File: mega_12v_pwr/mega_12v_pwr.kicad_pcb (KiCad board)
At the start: 2 copper layers, 170 x 144 mm, 48 parts, among them J1 Conn_01x01, J10 Conn_01x01, J11 Conn_01x01, J12 Conn_01x01, J13 Conn_01x01, J14 Conn_01x01, J15 Conn_01x01, J16 Conn_01x01, J17 Conn_01x01, J18 Conn_01x01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

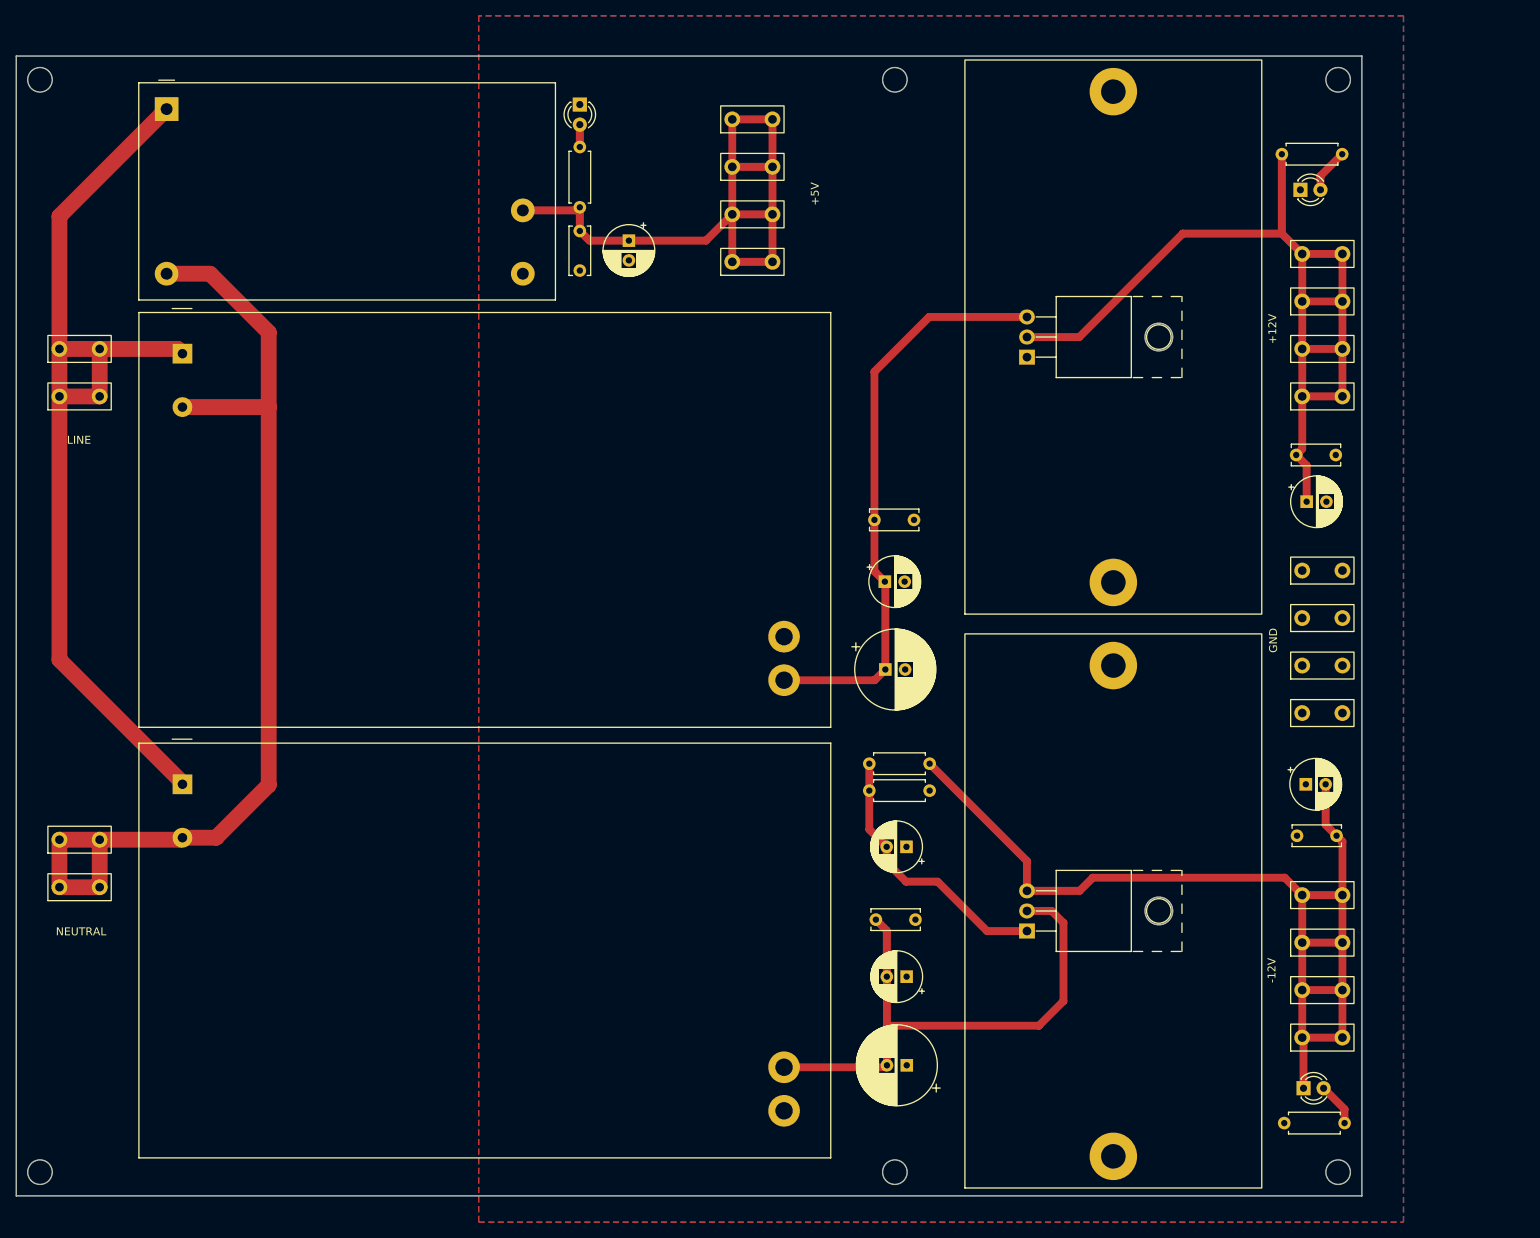
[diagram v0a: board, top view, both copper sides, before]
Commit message: Added fan connector
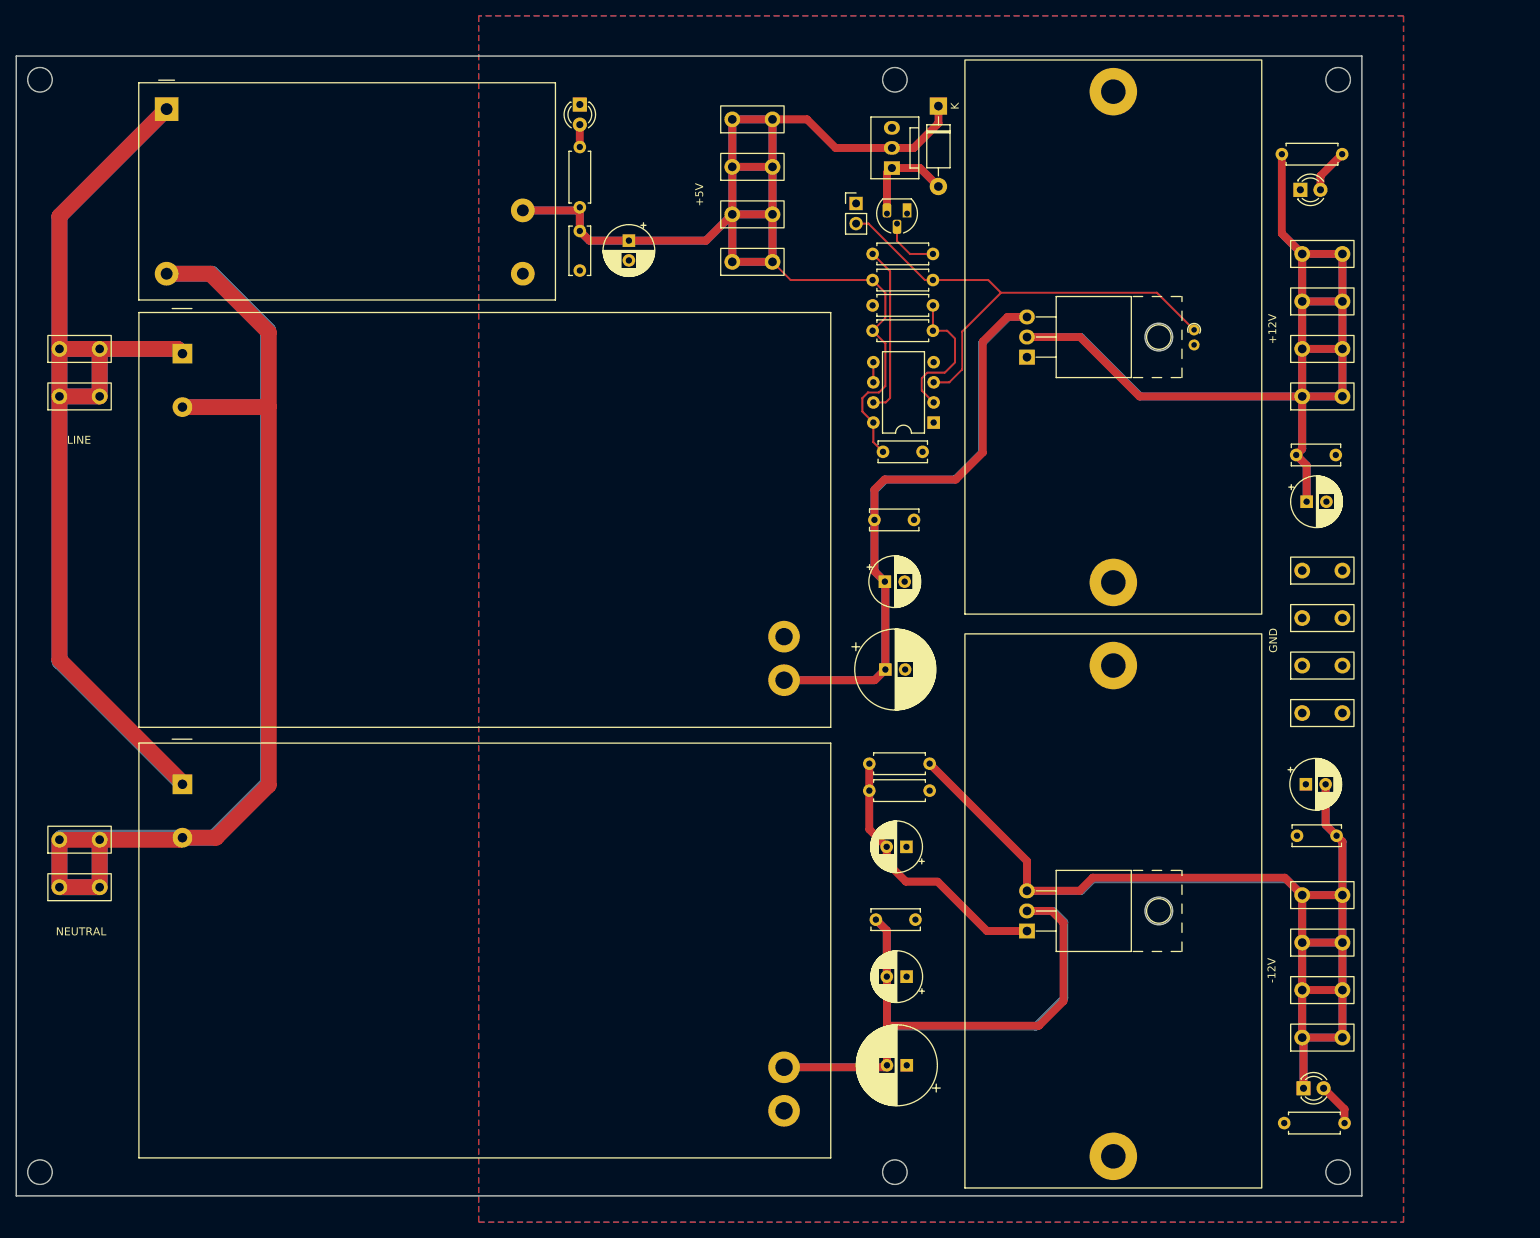
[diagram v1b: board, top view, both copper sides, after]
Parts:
- added C14: 100n, Capacitor_THT:C_Disc_D6.0mm_W2.5mm_P5.00mm, F.Cu at (143.5, 66.3)
- added D4: 1N4007, Diode_THT:D_DO-41_SOD81_P10.16mm_Horizontal, F.Cu at (150.5, 22.6)
- added J21: Conn_01x02, Connector_PinHeader_2.54mm:PinHeader_1x02_P2.54mm_Vertical, F.Cu at (140.1, 34.9)
- added M1: Fan_PC_Chassis, Connector:FanPinHeader_1x03_P2.54mm_Vertical, F.Cu at (144.6, 30.4)
- added Q1: 2N3904, Package_TO_SOT_THT:TO-92_HandSolder, F.Cu at (146.5, 36.2)
- added R6: 10k, Resistor_THT:R_Axial_DIN0207_L6.3mm_D2.5mm_P7.62mm_Horizontal, F.Cu at (142.2, 44.6)
- added R7: 10k, Resistor_THT:R_Axial_DIN0207_L6.3mm_D2.5mm_P7.62mm_Horizontal, F.Cu at (149.8, 47.8)
- added R8: 23k, Resistor_THT:R_Axial_DIN0207_L6.3mm_D2.5mm_P7.62mm_Horizontal, F.Cu at (142.2, 51.0)
- added R9: 470, Resistor_THT:R_Axial_DIN0207_L6.3mm_D2.5mm_P7.62mm_Horizontal, F.Cu at (142.2, 41.3)
- added TH1: 10k, Resistor_THT:R_Axial_DIN0204_L3.6mm_D1.6mm_P1.90mm_Vertical, F.Cu at (182.8, 50.9)
- added U3: LM311, Package_DIP:DIP-8_W7.62mm, F.Cu at (149.9, 62.6)
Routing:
- net +5V: track 87.8 -> 241.9 mm
- net NEUT: track 130.5 -> 260.7 mm
- net LINE: track 124.2 -> 248.4 mm
- net +12V: track 121.8 -> 233.5 mm
- net -12V: track 135.2 -> 244.0 mm
- net +15V: track 73.7 -> 146.1 mm
- net -15V: track 70.6 -> 141.5 mm
- net Net-(J21-Pin_2): track 0.00 -> 64.3 mm
- net Net-(R9-Pad1): track 0.00 -> 21.5 mm
- net Net-(U3-+): track 0.00 -> 18.1 mm
- net Net-(D4-A): track 0.00 -> 12.8 mm
- net Net-(Q1-B): track 0.00 -> 7.42 mm
- net Net-(U3-BAL): track 0.00 -> 2.54 mm

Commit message: Switched to PWM fan controller
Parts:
- removed Q1: 2N3904, Package_TO_SOT_THT:TO-92_HandSolder
- removed U3: LM311, Package_DIP:DIP-8_W7.62mm
- added C15: 1u, Capacitor_THT:C_Disc_D6.0mm_W2.5mm_P5.00mm, F.Cu at (149.9, 59.6)
- added C17: 10n, Capacitor_THT:C_Disc_D6.0mm_W2.5mm_P5.00mm, F.Cu at (145.7, 51.2)
- added Q2: IRLB8721PBF, Package_TO_SOT_THT:TO-220-3_Vertical, F.Cu at (151.9, 28.1)
- added R10: DNP, Resistor_THT:R_Axial_DIN0207_L6.3mm_D2.5mm_P7.62mm_Horizontal, F.Cu at (139.3, 44.8)
- added R11: 10k, Resistor_THT:R_Axial_DIN0207_L6.3mm_D2.5mm_P7.62mm_Horizontal, F.Cu at (146.9, 32.8)
- added U4: ~, Package_DIP:DIP-8_W7.62mm, F.Cu at (147.0, 62.2)
- R6: value 10k -> 2k
- R8: value 23k -> 27k
- R9: value 470 -> 100
- moved D4 16.4 mm to (134.7, 27.0), turned to 0 degrees
- moved J21 12.4 mm to (150.3, 41.9)
- moved M1 11.5 mm to (138.7, 20.6), turned to 180 degrees
- moved R8 9.65 mm to (139.3, 41.8)
- moved R7 9.46 mm to (146.9, 38.8)
- moved R9 7.25 mm to (146.9, 35.8), turned to 180 degrees
- moved R6 5.73 mm to (146.9, 47.9), turned to 180 degrees
- moved J15 3.91 mm to (123.1, 42.5)
- moved J16 3.91 mm to (123.1, 36.5)
- moved J17 3.91 mm to (123.1, 30.5)
- moved J18 3.91 mm to (123.1, 24.5)
- moved C14 2.91 mm to (140.6, 66.1)
- moved TH1 1.90 mm to (182.8, 52.8), turned to 90 degrees
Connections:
- J21 pad 1: GND -> +5V
- R6 pad 1: +5V -> Net-(J21-Pin_2)
- R6 pad 2: Net-(J21-Pin_2) -> GND
- TH1 pad 1: Net-(J21-Pin_2) -> +5V
- TH1 pad 2: GND -> Net-(J21-Pin_2)
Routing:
- net +5V: track 241.9 -> 333.7 mm
- net Net-(Q2-G): track 7.42 -> 17.6 mm
- net Net-(D4-A): track 12.8 -> 19.2 mm
- net Net-(U4-VOUT): track 21.5 -> 27.0 mm
- net +12V: track 233.5 -> 230.4 mm
- net Net-(J21-Pin_2): track 64.3 -> 67.2 mm
- net Net-(U4-CF): track 0.00 -> 2.92 mm
- net Net-(U4-VAS): track 18.1 -> 20.8 mm
- net Net-(U3-BAL): track 2.54 -> 0.00 mm

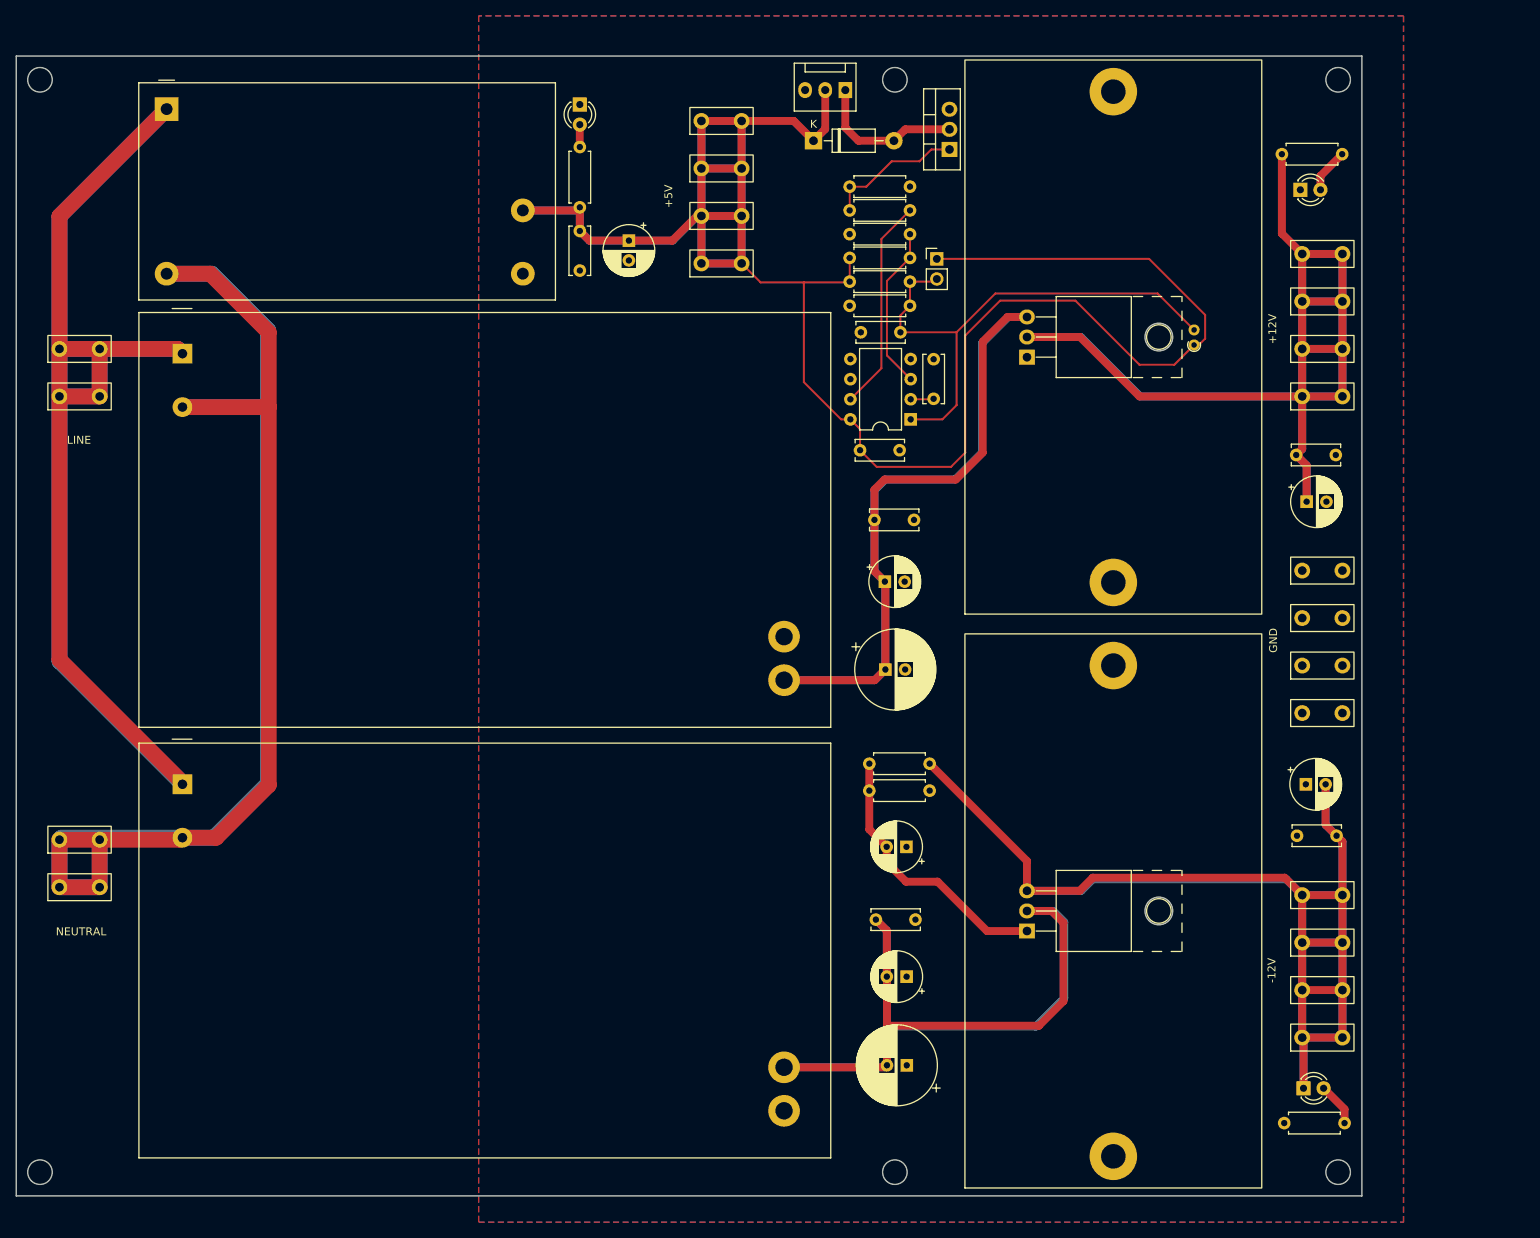
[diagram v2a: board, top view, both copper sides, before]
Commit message: Added more ground terminals
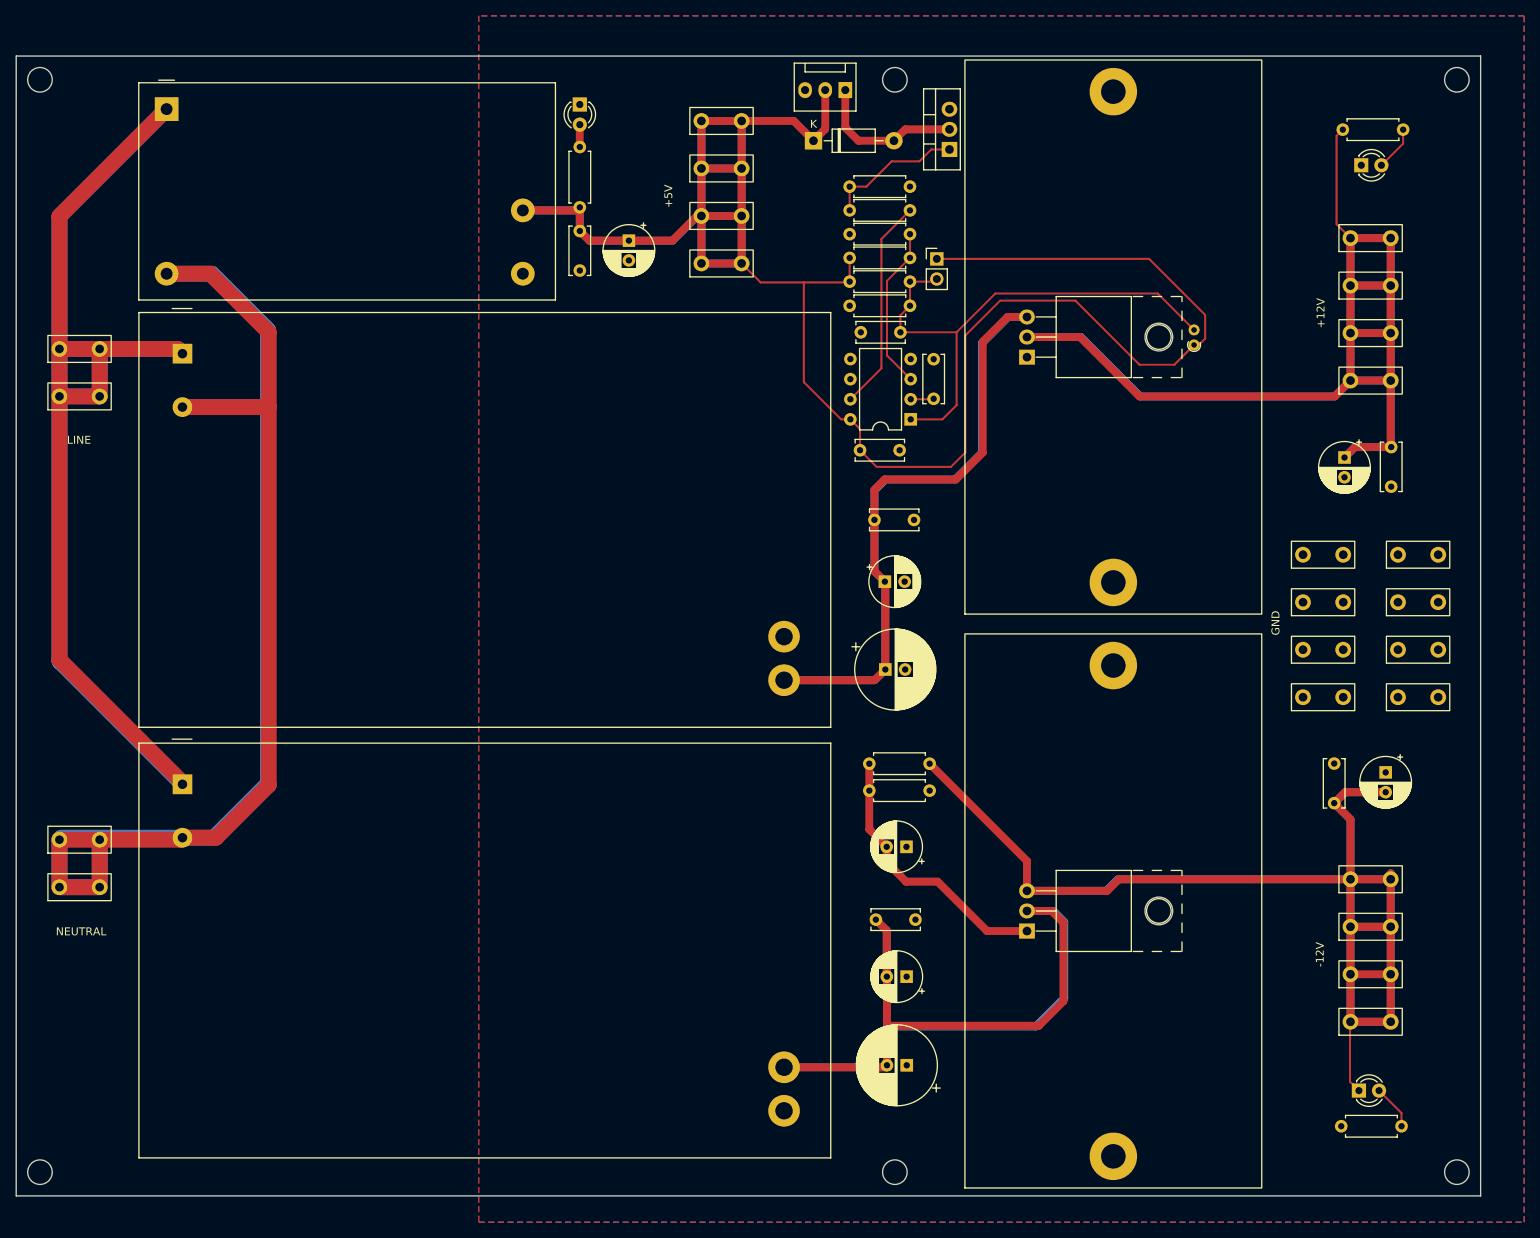
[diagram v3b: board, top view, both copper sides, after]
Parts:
- added J22: Conn_01x01, AlexCustom:SPADE, F.Cu at (211.1, 97.3)
- added J23: Conn_01x01, AlexCustom:SPADE, F.Cu at (211.1, 91.3)
- added J24: Conn_01x01, AlexCustom:SPADE, F.Cu at (211.1, 85.3)
- added J25: Conn_01x01, AlexCustom:SPADE, F.Cu at (211.1, 79.3)
- moved C10 12.0 mm to (207.7, 65.7), turned to -90 degrees
- moved C13 10.3 mm to (200.5, 105.7), turned to -90 degrees
- moved C4 10.2 mm to (207.0, 106.8), turned to -90 degrees
- moved D1 8.30 mm to (203.9, 30.1)
- moved R2 8.30 mm to (201.6, 25.6)
- moved C2 7.35 mm to (201.8, 67.0), turned to -90 degrees
- moved R4 7.21 mm to (201.4, 151.5)
- moved D3 7.01 mm to (203.6, 147.0)
- moved J13 6.42 mm to (205.1, 126.3)
- moved J11 6.42 mm to (205.1, 138.3)
- moved J12 6.42 mm to (205.1, 132.3)
- moved J14 6.42 mm to (205.1, 120.3)
- moved J3 6.42 mm to (205.1, 57.3)
- moved J4 6.42 mm to (205.1, 51.3)
- moved J5 6.42 mm to (205.1, 45.3)
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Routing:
- net +12V: track 230.4 -> 246.7 mm
- net -12V: track 244.0 -> 257.5 mm
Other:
- board size 170 x 144 mm -> 185 x 144 mm

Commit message: Updated resistor values
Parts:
- R1: value 120 -> 390
- R2, R4: value 2.2k -> 4.7k
- R3: value 1k -> 2.2k
- R5: value 860 -> 3.3k
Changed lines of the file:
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@@
         (effects (font (size 1 1) (thickness 0.15)))
     )
-    (fp_text value "120" (at 3.81 2.37) (layer "F.Fab")
+    (fp_text value "390" (at 3.81 2.37) (layer "F.Fab")
         (effects (font (size 1 1) (thickness 0.15)))
     )
@@
         (effects (font (size 1 1) (thickness 0.15)))
     )
-    (fp_text value "1k" (at 3.81 2.37 90) (layer "F.Fab")
+    (fp_text value "2.2k" (at 3.81 2.37 90) (layer "F.Fab")
         (effects (font (size 1 1) (thickness 0.15)))
     )
@@
         (effects (font (size 1 1) (thickness 0.15)))
     )
-    (fp_text value "2.2k" (at 3.81 2.37) (layer "F.Fab")
+    (fp_text value "4.7k" (at 3.81 2.37) (layer "F.Fab")
         (effects (font (size 1 1) (thickness 0.15)))
     )
@@
         (effects (font (size 1 1) (thickness 0.15)))
     )
-    (fp_text value "2.2k" (at 3.81 2.37) (layer "F.Fab")
+    (fp_text value "4.7k" (at 3.81 2.37) (layer "F.Fab")
         (effects (font (size 1 1) (thickness 0.15)))
     )
@@
         (effects (font (size 1 1) (thickness 0.15)))
     )
-    (fp_text value "860" (at 3.81 2.37) (layer "F.Fab")
+    (fp_text value "3.3k" (at 3.81 2.37) (layer "F.Fab")
         (effects (font (size 1 1) (thickness 0.15)))
     )
